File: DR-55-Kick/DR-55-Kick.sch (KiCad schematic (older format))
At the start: 19 parts

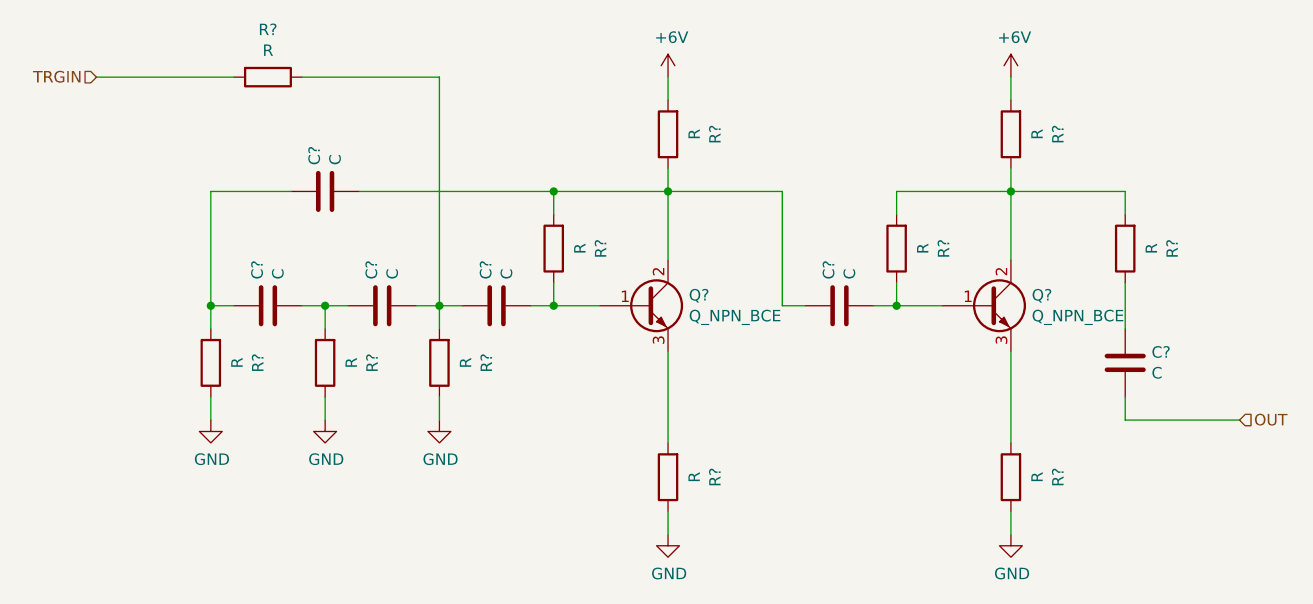
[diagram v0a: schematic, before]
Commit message: Added drums
Added all drum schematics.
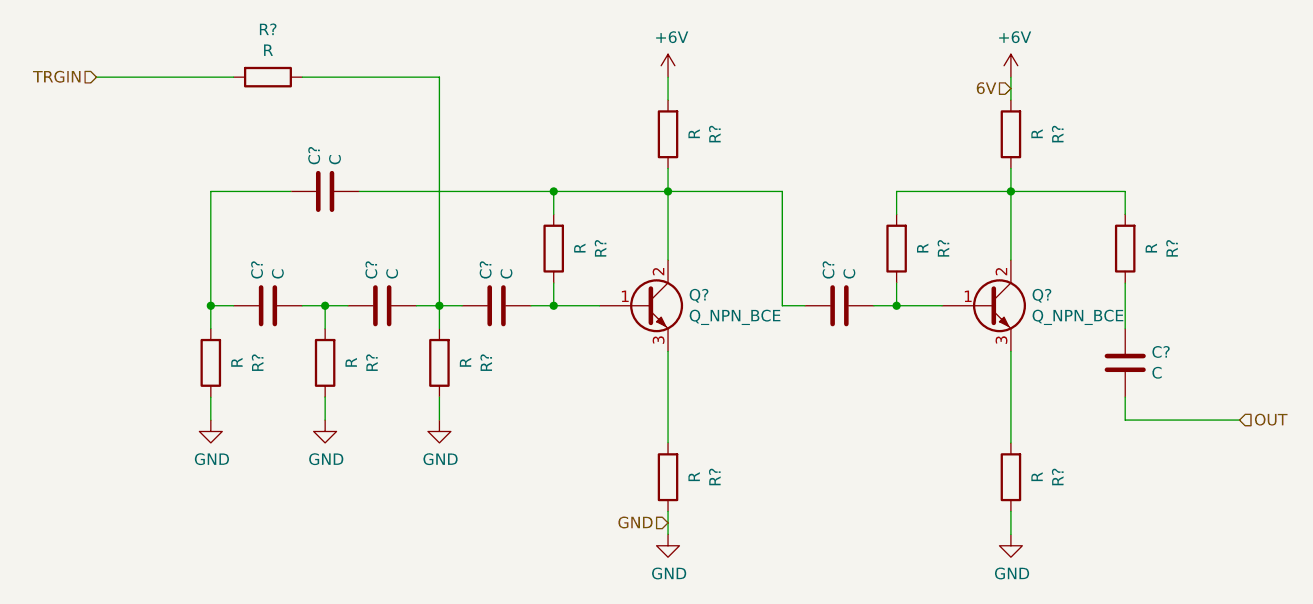
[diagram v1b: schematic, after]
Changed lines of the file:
@@
 $Descr A4 11693 8268
 encoding utf-8
-Sheet 1 3
+Sheet 2 6
 Title ""
 Date ""
@@
 Text HLabel 1500 1500 0    50   Input ~ 0
 TRGIN
+Text HLabel 5500 1550 0    50   Input ~ 0
+6V
+Text HLabel 4000 3450 0    50   Input ~ 0
+GND
 $EndSCHEMATC
